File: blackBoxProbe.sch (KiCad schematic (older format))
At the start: 81 parts, among them J1 USB-ID, J2 JTAG_2X05, J3 JTAG_2X05, J4 Conn_01x04, Q1 Q_NMOS_DUAL, Q2 Q_PMOS_DUAL, U1 MCP1702-MB, U2 USBLC6-2, U3 STM32F103CBT, U4 74X2T45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

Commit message: WIP: initial placement of all the components, start the tetris music!
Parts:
- removed C10: 100n, SquantorRcl:C_0603, symbol C
- Y1: value Crystal -> 8.000MHz
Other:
- moved on the sheet: C11, R10, R11
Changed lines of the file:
@@
 USB_D+
-$Comp
-L C C10
-U 1 1 5AC32A12
-P 2500 2650
-F 0 "C10" H 2525 2750 50  0000 L CNN
-F 1 "100n" H 2525 2550 50  0000 L CNN
-F 2 "SquantorRcl:C_0603" H 2538 2500 50  0001 C CNN
-F 3 "" H 2500 2650 50  0001 C CNN
-	1    2500 2650
-	0    1    1    0
-$EndComp
-$Comp
-L GND #PWR015
-U 1 1 5AC32ADA
-P 2300 2650
-F 0 "#PWR015" H 2300 2400 50  0001 C CNN
-F 1 "GND" H 2300 2500 50  0000 C CNN
-F 2 "" H 2300 2650 50  0001 C CNN
-F 3 "" H 2300 2650 50  0001 C CNN
-	1    2300 2650
-	0    1    1    0
-$EndComp
-$Comp
-L +5V #PWR016
-U 1 1 5AC32B15
-P 2700 2650
-F 0 "#PWR016" H 2700 2500 50  0001 C CNN
-F 1 "+5V" H 2700 2790 50  0000 C CNN
-F 2 "" H 2700 2650 50  0001 C CNN
-F 3 "" H 2700 2650 50  0001 C CNN
-	1    2700 2650
-	0    1    1    0
-$EndComp
 $Comp
 L STM32F103CBT U3
@@
 P 5550 6200
 F 0 "Y1" H 5550 6350 50  0000 C CNN
-F 1 "Crystal" H 5550 6050 50  0000 C CNN
+F 1 "8.000MHz" H 5550 6050 50  0000 C CNN
 F 2 "SquantorCrystal:SquantorCrystal-CRYSTAL_5.0X3.2" H 5550 6200 50  0001 C CNN
 F 3 "" H 5550 6200 50  0001 C CNN
@@
 L GND #PWR053
 U 1 1 5B224697
-P 2400 1750
-F 0 "#PWR053" H 2400 1500 50  0001 C CNN
-F 1 "GND" H 2400 1600 50  0000 C CNN
-F 2 "" H 2400 1750 50  0001 C CNN
-F 3 "" H 2400 1750 50  0001 C CNN
-	1    2400 1750
+P 3700 1700
+F 0 "#PWR053" H 3700 1450 50  0001 C CNN
+F 1 "GND" H 3700 1550 50  0000 C CNN
+F 2 "" H 3700 1700 50  0001 C CNN
+F 3 "" H 3700 1700 50  0001 C CNN
+	1    3700 1700
 	1    0    0    -1
 $EndComp
@@
 L C C11
 U 1 1 5B225142
-P 2400 1550
-F 0 "C11" H 2425 1650 50  0000 L CNN
-F 1 "100n" H 2425 1450 50  0000 L CNN
-F 2 "SquantorRcl:C_0603" H 2438 1400 50  0001 C CNN
-F 3 "" H 2400 1550 50  0001 C CNN
-	1    2400 1550
+P 3700 1500
+F 0 "C11" H 3725 1600 50  0000 L CNN
+F 1 "100n" H 3725 1400 50  0000 L CNN
+F 2 "SquantorRcl:C_0603" H 3738 1350 50  0001 C CNN
+F 3 "" H 3700 1500 50  0001 C CNN
+	1    3700 1500
 	-1   0    0    1
 $EndComp
@@
 L GND #PWR054
 U 1 1 5B225215
-P 2550 1750
-F 0 "#PWR054" H 2550 1500 50  0001 C CNN
-F 1 "GND" H 2550 1600 50  0000 C CNN
-F 2 "" H 2550 1750 50  0001 C CNN
-F 3 "" H 2550 1750 50  0001 C CNN
-	1    2550 1750
+P 3850 1700
+F 0 "#PWR054" H 3850 1450 50  0001 C CNN
+F 1 "GND" H 3850 1550 50  0000 C CNN
+F 2 "" H 3850 1700 50  0001 C CNN
+F 3 "" H 3850 1700 50  0001 C CNN
+	1    3850 1700
 	1    0    0    -1
 $EndComp
@@
 L R R11
 U 1 1 5B22528F
-P 2550 1550
-F 0 "R11" V 2630 1550 50  0000 C CNN
-F 1 "10K" V 2550 1550 50  0000 C CNN
-F 2 "SquantorRcl:R_0603_hand" V 2480 1550 50  0001 C CNN
-F 3 "" H 2550 1550 50  0001 C CNN
-	1    2550 1550
+P 3850 1500
+F 0 "R11" V 3930 1500 50  0000 C CNN
+F 1 "10K" V 3850 1500 50  0000 C CNN
+F 2 "SquantorRcl:R_0603_hand" V 3780 1500 50  0001 C CNN
+F 3 "" H 3850 1500 50  0001 C CNN
+	1    3850 1500
 	1    0    0    -1
 $EndComp
@@
 L R R10
 U 1 1 5B22537B
-P 2550 1150
-F 0 "R10" V 2630 1150 50  0000 C CNN
-F 1 "4.7K" V 2550 1150 50  0000 C CNN
-F 2 "SquantorRcl:R_0603_hand" V 2480 1150 50  0001 C CNN
-F 3 "" H 2550 1150 50  0001 C CNN
-	1    2550 1150
-	1    0    0    -1
-$EndComp
-Text Label 2700 1350 0    60   ~ 0
+P 3850 1100
+F 0 "R10" V 3930 1100 50  0000 C CNN
+F 1 "4.7K" V 3850 1100 50  0000 C CNN
+F 2 "SquantorRcl:R_0603_hand" V 3780 1100 50  0001 C CNN
+F 3 "" H 3850 1100 50  0001 C CNN
+	1    3850 1100
+	1    0    0    -1
+$EndComp
+Text Label 4000 1300 0    60   ~ 0
 TARGET_PWR_SENSE
-Text Label 2700 900  0    60   ~ 0
+Text Label 4000 850  0    60   ~ 0
 PROBE_VDD
 $Comp
@@
 	1800 3200 2100 3200
 Wire Wire Line
-	2650 2650 2700 2650
-Wire Wire Line
-	2350 2650 2300 2650
-Wire Wire Line
 	3950 4750 3850 4750
 Wire Wire Line
@@
 	9000 5900 8950 5900
 Wire Wire Line
-	2400 1750 2400 1700
-Wire Wire Line
-	2550 1700 2550 1750
-Wire Wire Line
-	2400 1400 2400 1350
-Wire Wire Line
-	2400 1350 2700 1350
-Wire Wire Line
-	2550 1300 2550 1400
-Connection ~ 2550 1350
-Wire Wire Line
-	2550 1000 2550 900
-Wire Wire Line
-	2550 900  2700 900
+	3700 1700 3700 1650
+Wire Wire Line
+	3850 1650 3850 1700
+Wire Wire Line
+	3700 1350 3700 1300
+Wire Wire Line
+	3700 1300 4000 1300
+Wire Wire Line
+	3850 1250 3850 1350
+Connection ~ 3850 1300
+Wire Wire Line
+	3850 950  3850 850
+Wire Wire Line
+	3850 850  4000 850
 Wire Wire Line
 	4400 7150 4500 7150

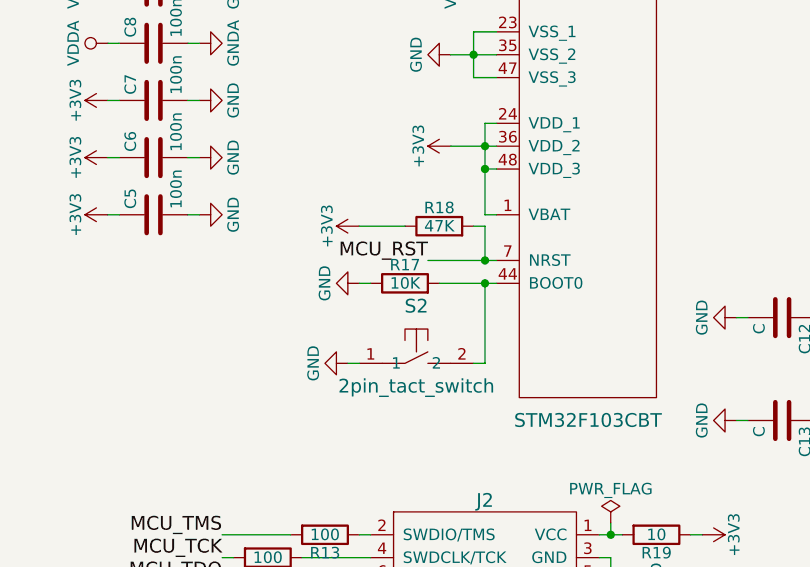
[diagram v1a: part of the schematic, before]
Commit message: FIX: fixed boot0 pulldown to something stronger WIP: further component placement WIP: need to replace JTAG headers to TH headers
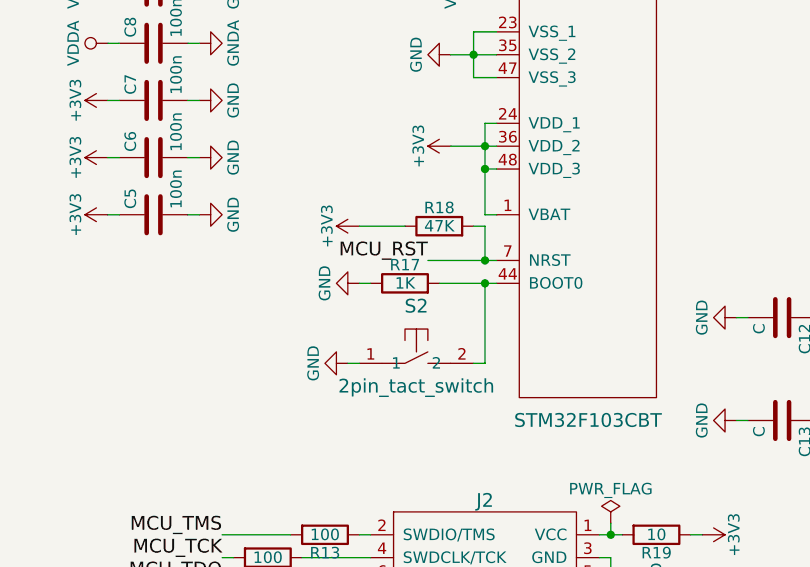
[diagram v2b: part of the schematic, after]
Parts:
- R17: value 10K -> 1K
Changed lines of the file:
@@
 P 3550 5850
 F 0 "R17" V 3630 5850 50  0000 C CNN
-F 1 "10K" V 3550 5850 50  0000 C CNN
+F 1 "1K" V 3550 5850 50  0000 C CNN
 F 2 "SquantorRcl:R_0603_hand" V 3480 5850 50  0001 C CNN
 F 3 "" H 3550 5850 50  0001 C CNN

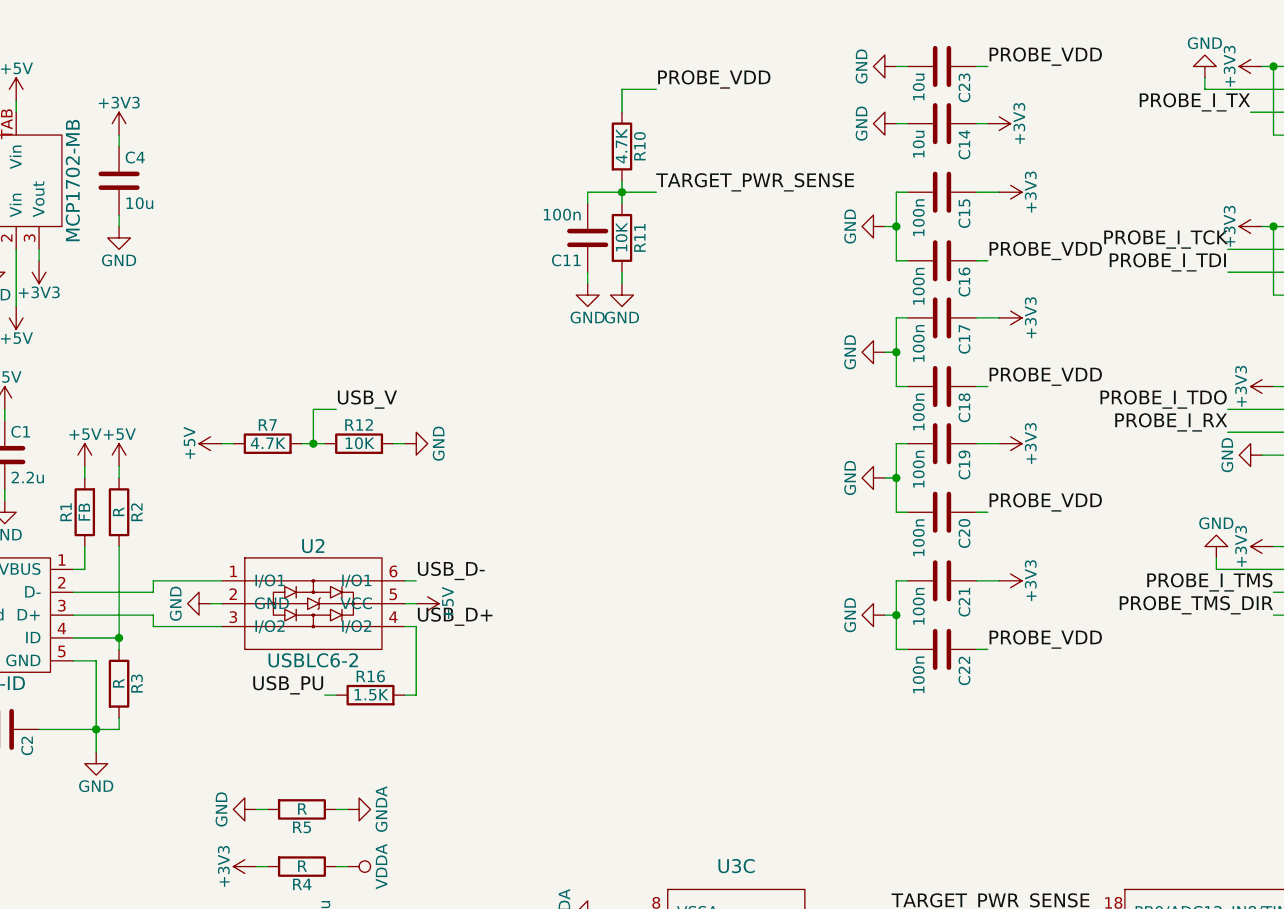
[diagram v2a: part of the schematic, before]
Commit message: DONE: tuned USB differential pair length WIP: inital layouting WIP: further optimal placing
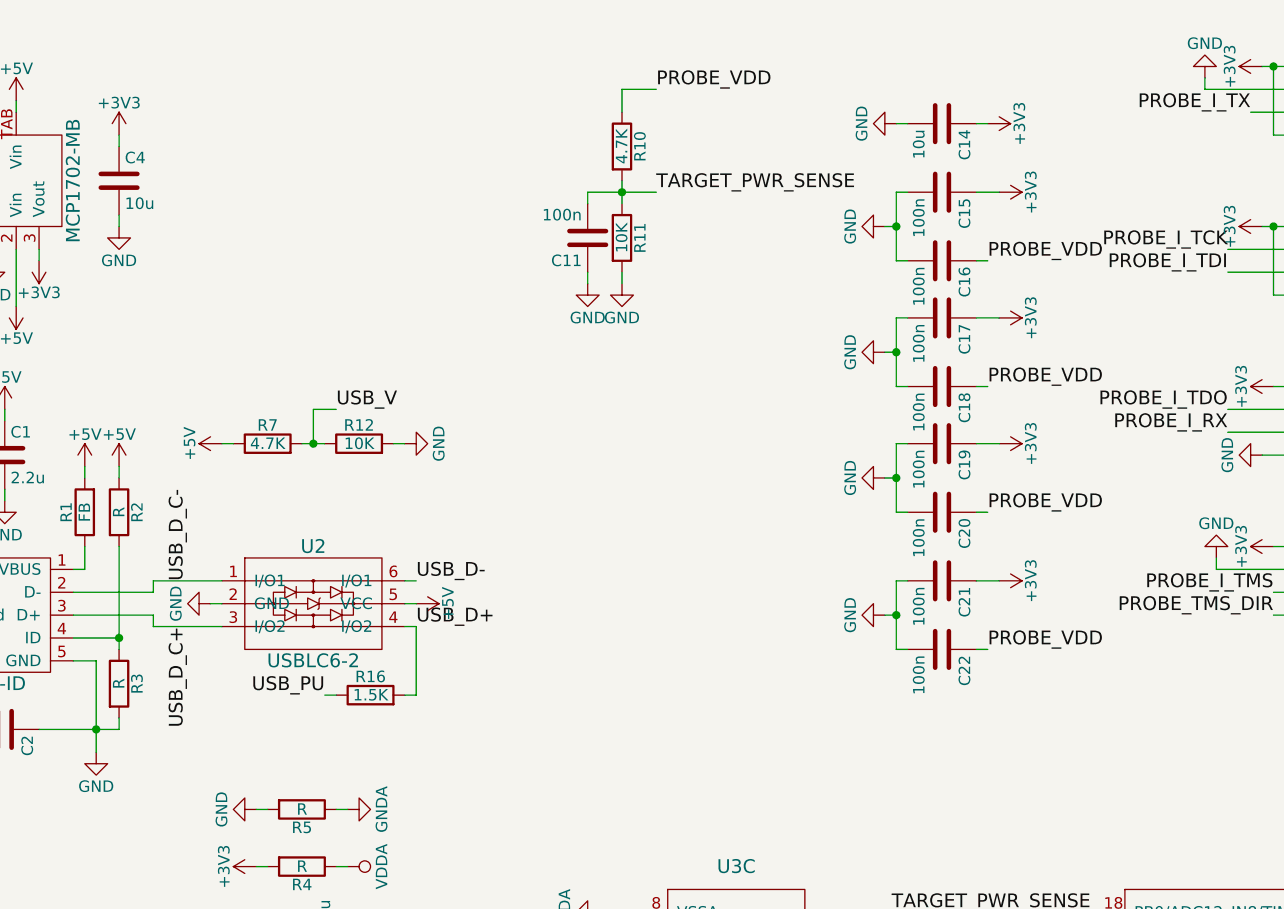
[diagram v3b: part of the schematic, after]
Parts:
- removed C23: 10u, SquantorRcl:C_0805, symbol C
- J2, J3: footprint SquantorConnectors:Header-0127-2X05-SMD -> SquantorConnectors:Header-0127-2X5-H006
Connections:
- net USB_D_C-: now reaches J1.2 (D-), U2.1 (I/O1)
- net USB_D_C+: now reaches J1.3 (D+), U2.3 (I/O2)

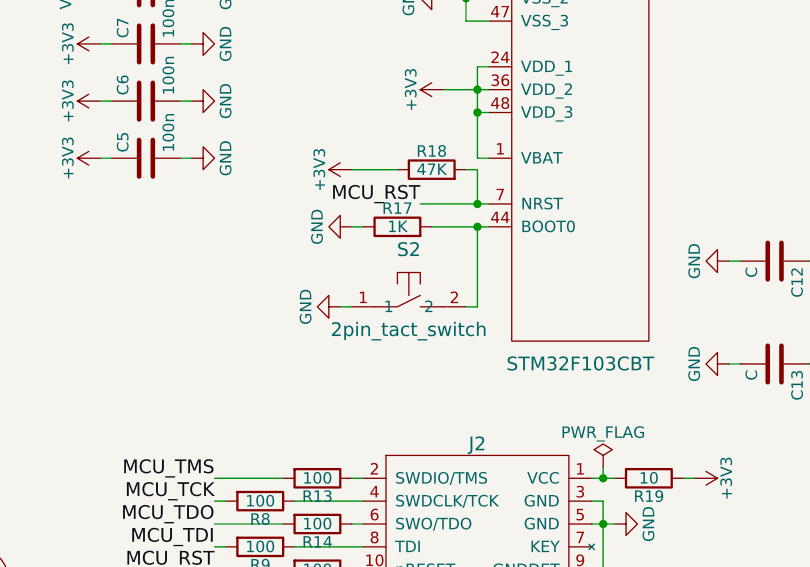
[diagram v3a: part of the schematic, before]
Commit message: WIP: More routing DONE: optimization of components, removing redudant/superflous components WIP: more optimal placement, maybe I can fit this in a 44 by 30mm box?
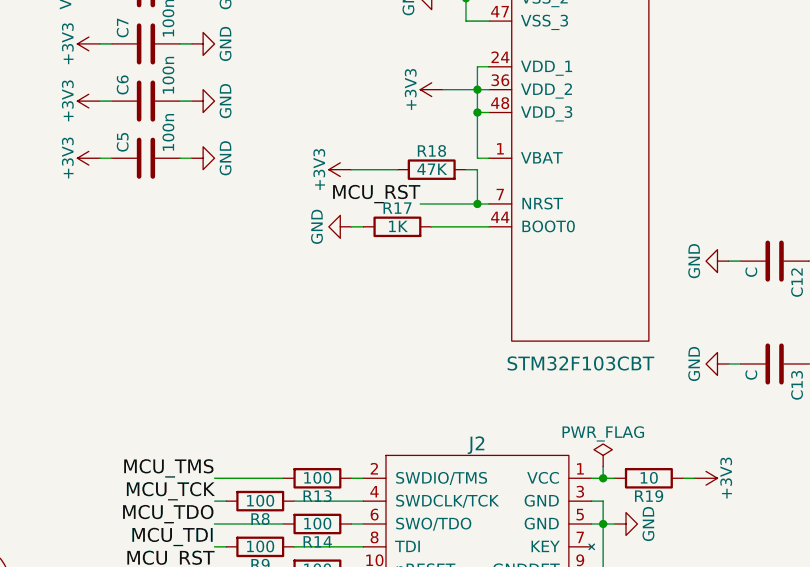
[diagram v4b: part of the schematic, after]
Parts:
- removed S2: 2pin_tact_switch, SquantorButtons:DTSM3, symbol 2pin_tact_switch
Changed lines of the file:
@@
 	0    -1   -1   0
-$EndComp
-$Comp
-L 2pin_tact_switch S2
-U 1 1 5B2168E0
-P 3600 6200
-F 0 "S2" H 3600 6450 60  0000 C CNN
-F 1 "2pin_tact_switch" H 3600 6100 60  0000 C CNN
-F 2 "SquantorButtons:DTSM3" H 3600 6200 60  0001 C CNN
-F 3 "" H 3600 6200 60  0001 C CNN
-	1    3600 6200
-	1    0    0    -1
-$EndComp
-$Comp
-L GND #PWR045
-U 1 1 5B2169F4
-P 3300 6200
-F 0 "#PWR045" H 3300 5950 50  0001 C CNN
-F 1 "GND" H 3300 6050 50  0000 C CNN
-F 2 "" H 3300 6200 50  0001 C CNN
-F 3 "" H 3300 6200 50  0001 C CNN
-	1    3300 6200
-	0    1    1    0
 $EndComp
 Text Label 8950 5800 2    60   ~ 0
@@
 	3400 5850 3350 5850
 Wire Wire Line
-	3900 5850 3900 6200
-Wire Wire Line
-	3900 6200 3850 6200
-Connection ~ 3900 5850
-Wire Wire Line
-	3350 6200 3300 6200
-Wire Wire Line
 	9000 5700 8950 5700

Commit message: WIP: additional routing WIP: placed the level shifting network WIP: Further component optimization and removal
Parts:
- removed R27: 100, SquantorRcl:R_0603_hand, symbol R
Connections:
- net PROBE_E_VDD is gone; now on net PROBE_VDD: R20.1

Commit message: FIX: incorrect pin mapping of STM32 DONE: changed to 3mm leds, plenty of space DONE: routing WIP: Silk/value placing
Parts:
- D1, D2, D3, D4: footprint LEDs:LED_PLCC-2 -> LEDs:LED_D3.0mm
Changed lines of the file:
@@
 F 0 "D1" H 950 6000 50  0000 C CNN
 F 1 "Green" H 950 5800 50  0000 C CNN
-F 2 "LEDs:LED_PLCC-2" H 950 5900 50  0001 C CNN
+F 2 "LEDs:LED_D3.0mm" H 950 5900 50  0001 C CNN
 F 3 "" H 950 5900 50  0001 C CNN
 	1    950  5900
@@
 F 0 "D2" H 950 6300 50  0000 C CNN
 F 1 "Yellow" H 950 6100 50  0000 C CNN
-F 2 "LEDs:LED_PLCC-2" H 950 6200 50  0001 C CNN
+F 2 "LEDs:LED_D3.0mm" H 950 6200 50  0001 C CNN
 F 3 "" H 950 6200 50  0001 C CNN
 	1    950  6200
@@
 F 0 "D3" H 950 6600 50  0000 C CNN
 F 1 "Orange" H 950 6400 50  0000 C CNN
-F 2 "LEDs:LED_PLCC-2" H 950 6500 50  0001 C CNN
+F 2 "LEDs:LED_D3.0mm" H 950 6500 50  0001 C CNN
 F 3 "" H 950 6500 50  0001 C CNN
 	1    950  6500
@@
 F 0 "D4" H 950 6900 50  0000 C CNN
 F 1 "Red" H 950 6700 50  0000 C CNN
-F 2 "LEDs:LED_PLCC-2" H 950 6800 50  0001 C CNN
+F 2 "LEDs:LED_D3.0mm" H 950 6800 50  0001 C CNN
 F 3 "" H 950 6800 50  0001 C CNN
 	1    950  6800

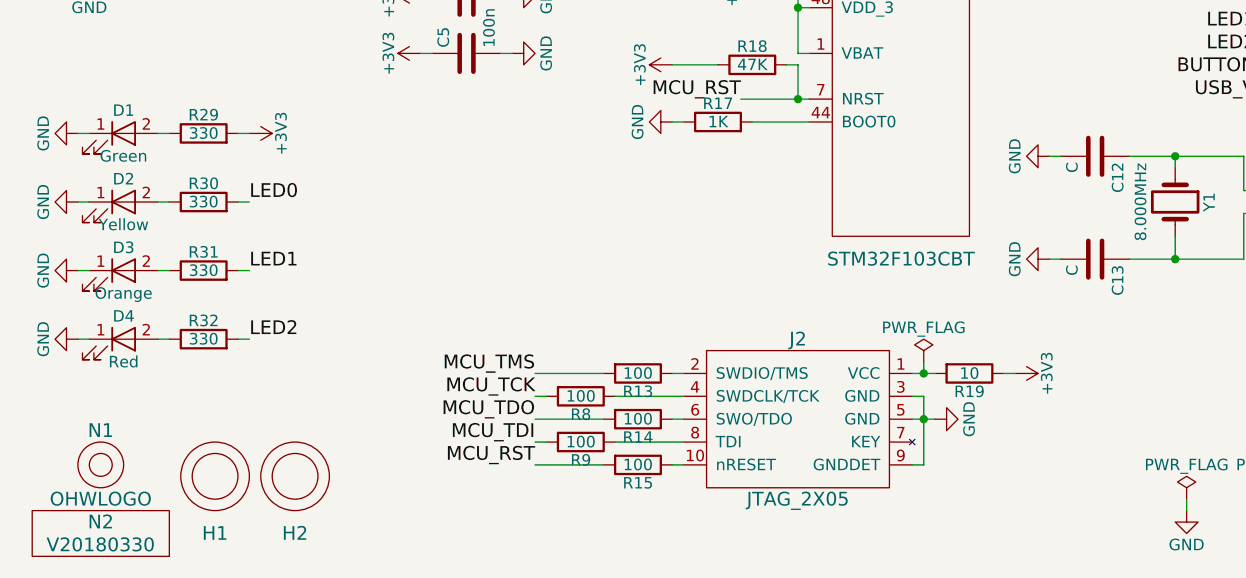
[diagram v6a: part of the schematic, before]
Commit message: DONE: fixed crystal layout DONE: added a guard trace to isolate crystal from VSSA
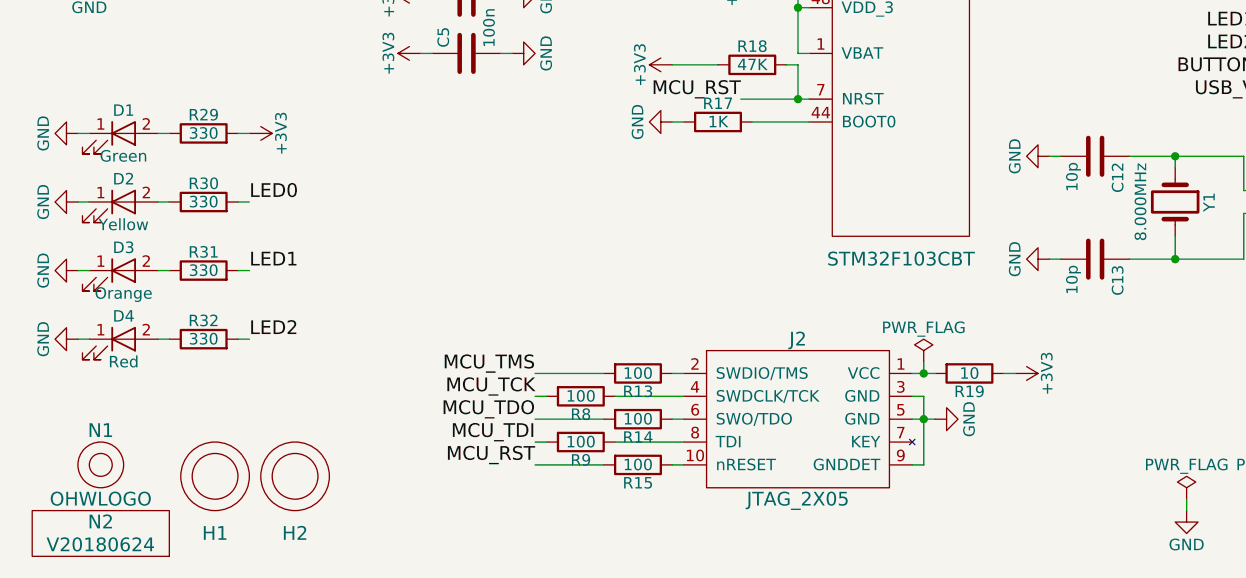
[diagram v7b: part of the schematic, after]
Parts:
- C12, C13: value C -> 10p
- N2: value V20180330 -> V20180624
- Y1: footprint SquantorCrystal:SquantorCrystal-CRYSTAL_5.0X3.2 -> SquantorCrystal:X_5.0_3.2
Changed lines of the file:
@@
 P 850 7700
 F 0 "N2" H 850 7800 60  0000 C CNN
-F 1 "V20180330" H 850 7700 60  0000 C CNN
+F 1 "V20180624" H 850 7700 60  0000 C CNN
 F 2 "SquantorLabels:Label_version" H 850 7700 60  0001 C CNN
 F 3 "" H 850 7700 60  0001 C CNN
@@
 F 0 "Y1" H 5550 6350 50  0000 C CNN
 F 1 "8.000MHz" H 5550 6050 50  0000 C CNN
-F 2 "SquantorCrystal:SquantorCrystal-CRYSTAL_5.0X3.2" H 5550 6200 50  0001 C CNN
+F 2 "SquantorCrystal:X_5.0_3.2" H 5550 6200 50  0001 C CNN
 F 3 "" H 5550 6200 50  0001 C CNN
 	1    5550 6200
@@
 P 5200 6000
 F 0 "C12" H 5225 6100 50  0000 L CNN
-F 1 "C" H 5225 5900 50  0000 L CNN
+F 1 "10p" H 5225 5900 50  0000 L CNN
 F 2 "SquantorRcl:C_0603" H 5238 5850 50  0001 C CNN
 F 3 "" H 5200 6000 50  0001 C CNN
@@
 P 5200 6450
 F 0 "C13" H 5225 6550 50  0000 L CNN
-F 1 "C" H 5225 6350 50  0000 L CNN
+F 1 "10p" H 5225 6350 50  0000 L CNN
 F 2 "SquantorRcl:C_0603" H 5238 6300 50  0001 C CNN
 F 3 "" H 5200 6450 50  0001 C CNN
